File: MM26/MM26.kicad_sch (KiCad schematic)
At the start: 3 parts, among them U1 AZ1117IH-3.3TRG1

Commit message: imported MCU to KiCAD
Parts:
- added U2: NUCLEO-L476RG, NUCLEO-L476RG:MODULE_NUCLEO-L476RG, symbol NUCLEO-L476RG:NUCLEO-L476RG

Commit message: power
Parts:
- added J1, J2: B2B-PH-K-S, B2B-PH-K-S:JST_B2B-PH-K-S, symbol B2B-PH-K-S:B2B-PH-K-S
- added SW1: CL-SB-12A-01T, CL-SB-12A-01T_NDC, symbol CL_SB_12A_01T:CL-SB-12A-01T
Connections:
- net +BATT: now also SW1.2
- net GND: now also J2.2, SW1.1
- new net: J1.2, J2.1
- new net: J1.1, SW1.3

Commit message: Imported Everything
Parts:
- added J3, J4: Conn_01x06_Pin, Connector_JST:JST_SH_BM06B-SRSS-TB_1x06-1MP_P1.00mm_Vertical, symbol Connector:Conn_01x06_Pin
- added J5, J6, J7, J8, J9: Conn_01x03_Pin, Connector_PinSocket_2.54mm:PinSocket_1x03_P2.54mm_Horizontal, symbol Connector:Conn_01x03_Pin
- added R1: 10k, symbol Device:R
- added U3: ISM330DHCX, Adafruit_ISM330DHCX:ISM330DHCX, symbol Adafruit_ISM330DHCX:ISM330DHCX
- added U4: SSD1306, Adafruit_SSD1306:SSD1306, symbol Adafruit_SSD1306:SSD1306
- added U5: L293DD, L293DD:SOIC127P1032X265-20N, symbol L293DD:L293DD
- J1, J2: footprint B2B-PH-K-S:JST_B2B-PH-K-S -> B2B_PH_K_S:JST_B2B-PH-K-S
- SW1: footprint CL-SB-12A-01T_NDC -> CL_SB_12A_01T:CL-SB-12A-01T_NDC
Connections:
- net +BATT: now also R1.1
- net GND: now also J5.2 (Pin_2), J6.2 (Pin_2), J7.2 (Pin_2), J8.2 (Pin_2), J9.2 (Pin_2), R1.2
- net VCC: now also J5.3 (Pin_3), J6.3 (Pin_3), J7.3 (Pin_3), J8.3 (Pin_3), J9.3 (Pin_3)

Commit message: H Bridge Wiring
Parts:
- added C3, C5: 4.7uF, symbol Device:C
- added C4: 100nF, symbol Device:C
- added C6: 10uF, symbol Device:C
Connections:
- net +BATT: now also U5.20 (VSS), C3.1, C4.1
- net GND: now also J3.6 (Pin_6), J4.6 (Pin_6), U5.14 (GND__4), U5.15 (GND__5), U5.16 (GND__6), U5.17 (GND__7), U5.4 (GND), U5.5 (GND__1), U5.6 (GND__2), U5.7 (GND__3), C3.2, C4.2, C5.2, C6.2
- net VCC: now also J3.3 (Pin_3), J4.3 (Pin_3), U5.1 (ENABLE_1), U5.10 (VS), U5.11 (ENABLE_2), C5.1, C6.1
- net M+2: now reaches J4.1 (Pin_1)
- net M+2: now also U5.13 (OUTPUT_3)
- net M-2: now reaches J4.2 (Pin_2)
- net M-2: now also U5.18 (OUTPUT_4)
- net ENC2_A: now reaches J4.4 (Pin_4)
- net ENC2_B: now reaches J4.5 (Pin_5)
- net M+1: now reaches U5.3 (OUTPUT_1)
- net M+1: now also J3.1 (Pin_1)
- net M-1: now reaches U5.8 (OUTPUT_2)
- net M-1: now also J3.2 (Pin_2)
- net ENC1_A: now reaches J3.4 (Pin_4)
- net ENC1_B: now reaches J3.5 (Pin_5)
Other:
- moved on the sheet: J3, J4, J5, J6, J7, J8, J9, U2A, U2B, U5

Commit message: good enough schematic
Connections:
- net ENC1_A: now also U2.CN7_28 (PA0)
- net ENC1_B: now also U2.CN7_30 (PA1)
- net ENC2_A: now also U2.CN10_15 (PA7)
- net ENC2_B: now also U2.CN10_13 (PA6)
- net GND: now also U2.CN7_5 (VDD), U3.14 (GND), U3.3 (GND), U4.8 (GND)
- net VCC: now also U2.CN7_16 (+3V3), U3.1 (Vin), U4.6 (VIN)
- net IR_OUT_3: now reaches J9.1 (Pin_1)
- net IR_OUT_3: now also U2.CN10_26 (PB15)
- net Gyro_SCL: now reaches U2.CN7_1 (PC10)
- net Gyro_SCL: now also U3.4 (SCL)
- net Gyro_MISO: now reaches U2.CN7_2 (PC11)
- net Gyro_MISO: now also U3.6 (MISO)
- net Gyro_MOSI: now reaches U2.CN7_3 (PC12)
- net Gyro_MOSI: now also U3.5 (SDA/MOSI)
- net Gyro_CS: now reaches U2.CN7_32 (PA4)
- net Gyro_CS: now also U3.7 (CS)
- net OLED_MISO: now reaches U2.CN7_35 (PC2)
- net OLED_MISO: now also U4.3 (D/C)
- net OLED_MOSI: now reaches U2.CN7_37 (PC3)
- net OLED_MOSI: now also U4.5 (DATA)
- net IR_OUT_5: now reaches J8.1 (Pin_1)
- net IR_OUT_5: now also U2.CN10_34 (PC4)
- net IR_OUT_1: now reaches J5.1 (Pin_1)
- net IR_OUT_1: now also U2.CN10_24 (PB1)
- net M1_C: now reaches U2.CN10_14 (PA11)
- net M1_C: now also U5.2 (INPUT_1)
- net OLED_CS: now reaches U2.CN10_16 (PB12)
- net OLED_CS: now also U4.1 (CS)
- net M2_C: now reaches U2.CN10_21 (PA9)
- net M2_C: now also U5.12 (INPUT_3)
- net IR_OUT_2: now reaches U2.CN10_22 (PB2)
- net IR_OUT_2: now also J7.1 (Pin_1)
- net M2_CC: now reaches U2.CN10_23 (PA8)
- net M2_CC: now also U5.19 (INPUT_4)
- net IR_OUT_4: now reaches U2.CN10_28 (PB14)
- net IR_OUT_4: now also J6.1 (Pin_1)
- net OLED_SCL: now reaches U2.CN10_30 (PB13)
- net OLED_SCL: now also U4.4 (CLK)
- net M1_CC: now reaches U2.CN10_33 (PA10)
- net M1_CC: now also U5.9 (INPUT_2)
- no-connect marks 0 -> 10
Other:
- moved on the sheet: U2A, U2B, U3, U4

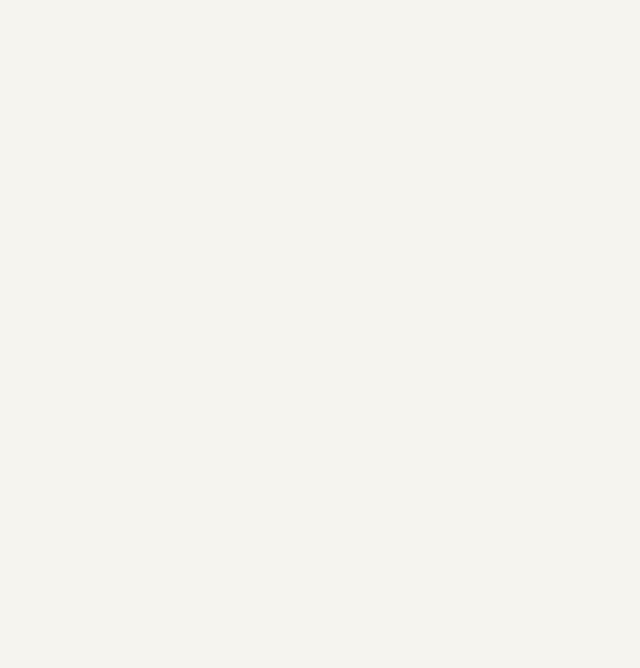
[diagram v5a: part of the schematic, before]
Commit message: all components placed on pcb
just need to route it now
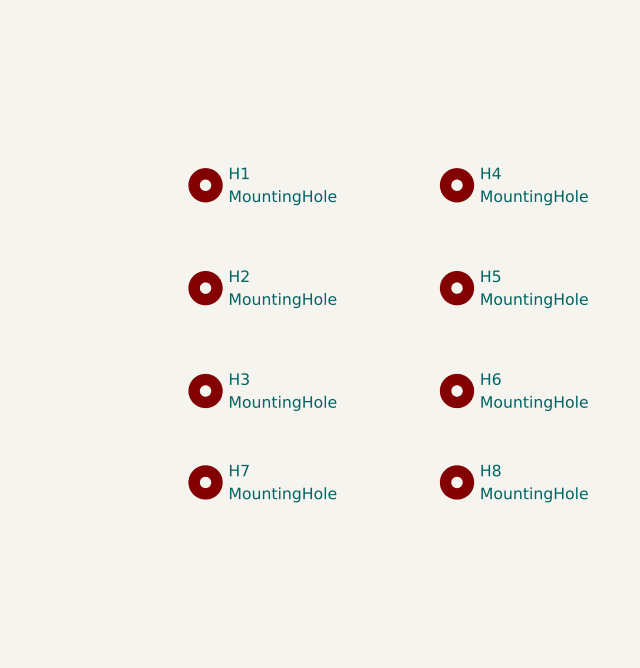
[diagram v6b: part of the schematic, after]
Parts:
- added H1, H2, H3, H4, H5, H6: MountingHole, MountingHole:MountingHole_2.5mm, symbol Mechanical:MountingHole
- added H7, H8: MountingHole, MountingHole:MountingHole_2mm, symbol Mechanical:MountingHole
- C1, C2, C3, C4, C5, C6: footprint (none) -> Capacitor_SMD:C_0805_2012Metric_Pad1.18x1.45mm_HandSolder
- R1: footprint (none) -> Resistor_SMD:R_0805_2012Metric_Pad1.20x1.40mm_HandSolder

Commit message: pcb done
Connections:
- net VCC: now also U3.2 (3V3), U4.7 (3V3); no longer U3.1 (Vin), U4.6 (VIN)
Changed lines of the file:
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@@
 	(text_box "OLED"
 		(exclude_from_sim no)
-		(at 92.71 21.59 0)
+		(at 93.98 24.13 0)
 		(size 44.45 60.96)
+		(margins 0.9525 0.9525 0.9525 0.9525)
+		(stroke
+			(width 0)
+			(type solid)
+		)
+		(fill
+			(type none)
+		)
+		(effects
+			(font
+				(size 1.27 1.27)
+			)
+			(justify right top)
+		)
+	)
+	(text_box "Motors"
+		(exclude_from_sim no)
+		(at 22.86 200.66 0)
+		(size 127 68.58)
 		(margins 0.9525 0.9525 0.9525 0.9525)
 		(stroke
@@
 		)
 	)
-	(text_box "Motors"
+	(text_box "POWER"
 		(exclude_from_sim no)
-		(at 22.86 200.66 0)
-		(size 127 68.58)
+		(at 21.59 139.7 0)
+		(size 81.28 48.26)
 		(margins 0.9525 0.9525 0.9525 0.9525)
 		(stroke
@@
 		)
 	)
-	(text_box "POWER"
+	(text_box "IMU"
 		(exclude_from_sim no)
-		(at 21.59 139.7 0)
-		(size 81.28 48.26)
+		(at 29.21 26.67 0)
+		(size 53.34 48.26)
 		(margins 0.9525 0.9525 0.9525 0.9525)
 		(stroke
@@
 		)
 	)
-	(text_box "IMU"
+	(text_box "IR Sensors"
 		(exclude_from_sim no)
-		(at 29.21 26.67 0)
-		(size 53.34 48.26)
+		(at 116.84 120.65 0)
+		(size 81.28 59.69)
 		(margins 0.9525 0.9525 0.9525 0.9525)
 		(stroke
@@
 		)
 	)
-	(text_box "IR Sensors"
+	(text_box "3V3 Regulator"
 		(exclude_from_sim no)
-		(at 116.84 120.65 0)
-		(size 81.28 59.69)
+		(at 21.59 86.36 0)
+		(size 73.66 46.99)
 		(margins 0.9525 0.9525 0.9525 0.9525)
 		(stroke
@@
 		)
 	)
-	(text_box "3V3 Regulator"
-		(exclude_from_sim no)
-		(at 21.59 86.36 0)
-		(size 73.66 46.99)
-		(margins 0.9525 0.9525 0.9525 0.9525)
-		(stroke
-			(width 0)
-			(type solid)
-		)
-		(fill
-			(type none)
-		)
-		(effects
-			(font
-				(size 1.27 1.27)
-			)
-			(justify left top)
-		)
-	)
 	(junction
 		(at 114.3 222.25)
@@
 	)
 	(no_connect
-		(at 43.18 44.45)
+		(at 43.18 41.91)
+	)
+	(no_connect
+		(at 116.84 59.69)
 	)
 	(no_connect
@@
 	)
 	(no_connect
-		(at 116.84 63.5)
-	)
-	(no_connect
 		(at 67.31 48.26)
 	)
@@
 	(wire
 		(pts
-			(xy 124.46 58.42) (xy 124.46 59.69)
-		)
-		(stroke
-			(width 0)
-			(type default)
-		)
-	)
-	(wire
-		(pts
 			(xy 72.39 121.92) (xy 81.28 121.92)
 		)
@@
 	(wire
 		(pts
+			(xy 124.46 58.42) (xy 124.46 63.5)
+		)
+		(stroke
+			(width 0)
+			(type default)
+		)
+	)
+	(wire
+		(pts
 			(xy 209.55 40.64) (xy 204.47 40.64)
 		)
@@
 	(wire
 		(pts
-			(xy 39.37 38.1) (xy 39.37 41.91)
+			(xy 39.37 38.1) (xy 39.37 44.45)
 		)
 		(stroke
@@
 	(wire
 		(pts
-			(xy 39.37 41.91) (xy 43.18 41.91)
-		)
-		(stroke
-			(width 0)
-			(type default)
-		)
-	)
-	(wire
-		(pts
 			(xy 54.61 121.92) (xy 54.61 124.46)
 		)
@@
 	(wire
 		(pts
+			(xy 43.18 44.45) (xy 39.37 44.45)
+		)
+		(stroke
+			(width 0)
+			(type default)
+		)
+	)
+	(wire
+		(pts
 			(xy 76.2 107.95) (xy 81.28 107.95)
 		)
@@
 	(wire
 		(pts
+			(xy 124.46 63.5) (xy 116.84 63.5)
+		)
+		(stroke
+			(width 0)
+			(type default)
+		)
+	)
+	(wire
+		(pts
 			(xy 118.11 222.25) (xy 114.3 222.25)
 		)
@@
 		)
 		(stroke
-			(width 0)
-			(type default)
-		)
-	)
-	(wire
-		(pts
-			(xy 124.46 59.69) (xy 116.84 59.69)
-		)
-		(stroke
